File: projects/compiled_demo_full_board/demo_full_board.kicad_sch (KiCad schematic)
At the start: 16 parts, among them U1 ATmega328, U2 LM7805, Y1 16MHz

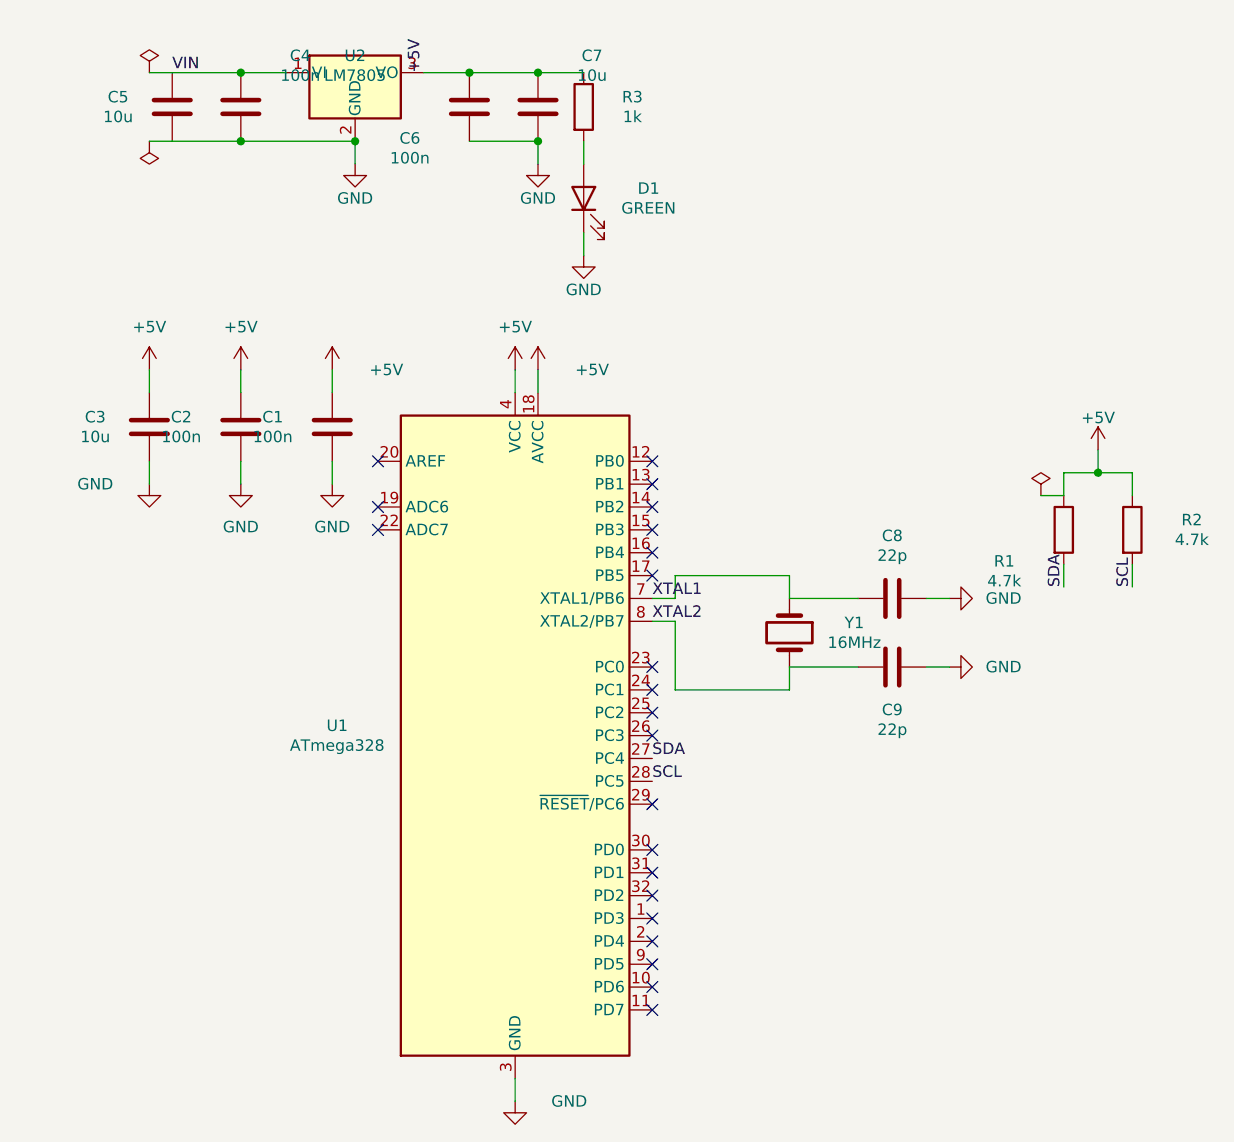
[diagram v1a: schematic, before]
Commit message: Body model sees real symbol graphics; quiet nets drop junction tags
User-reported flaws from visual review, both fixed at the root:

- Wires over symbol artwork: the body model was pin-derived and blind to
  drawn graphics — an op-amp triangle's vertices stick out beyond the pin
  box, so "legal" wires crossed the drawing. internal/sexp/graphics.go now
  parses rectangle/polyline/circle/arc/bezier extents per unit with the
  exact pin transform; metrics.BodyBBox unions them with the legacy box,
  clamped off pin tips (Device:LED's emission arrows overhang the cathode
  pin and would have swallowed it). NE5532 feedback: 8 stroke crossings
  through the triangle before, 0 after (loops now label pairs). The model
  also exposed genuinely bad baked geometry in mcu_minimal_atmega328's
  crystal — repositioned with the template contract intact.

- "ANODE" tag on a resistor leg: net names with a "_" prefix are now
  quiet — connectivity only, their documentation label is stripped at the
  end of compilation when the wiring alone keeps the net whole. Junction
  nodes (R->LED) stay unlabeled like in any hand-drawn schematic.

- Battery hump: led_18650 anchors R1 in the pin's exit direction; the
  design guide gains the "respect the pin's exit direction" and "internal
  junctions carry no tag" recipes.

Co-Authored-By: Claude Fable 5 <noreply@anthropic.com>
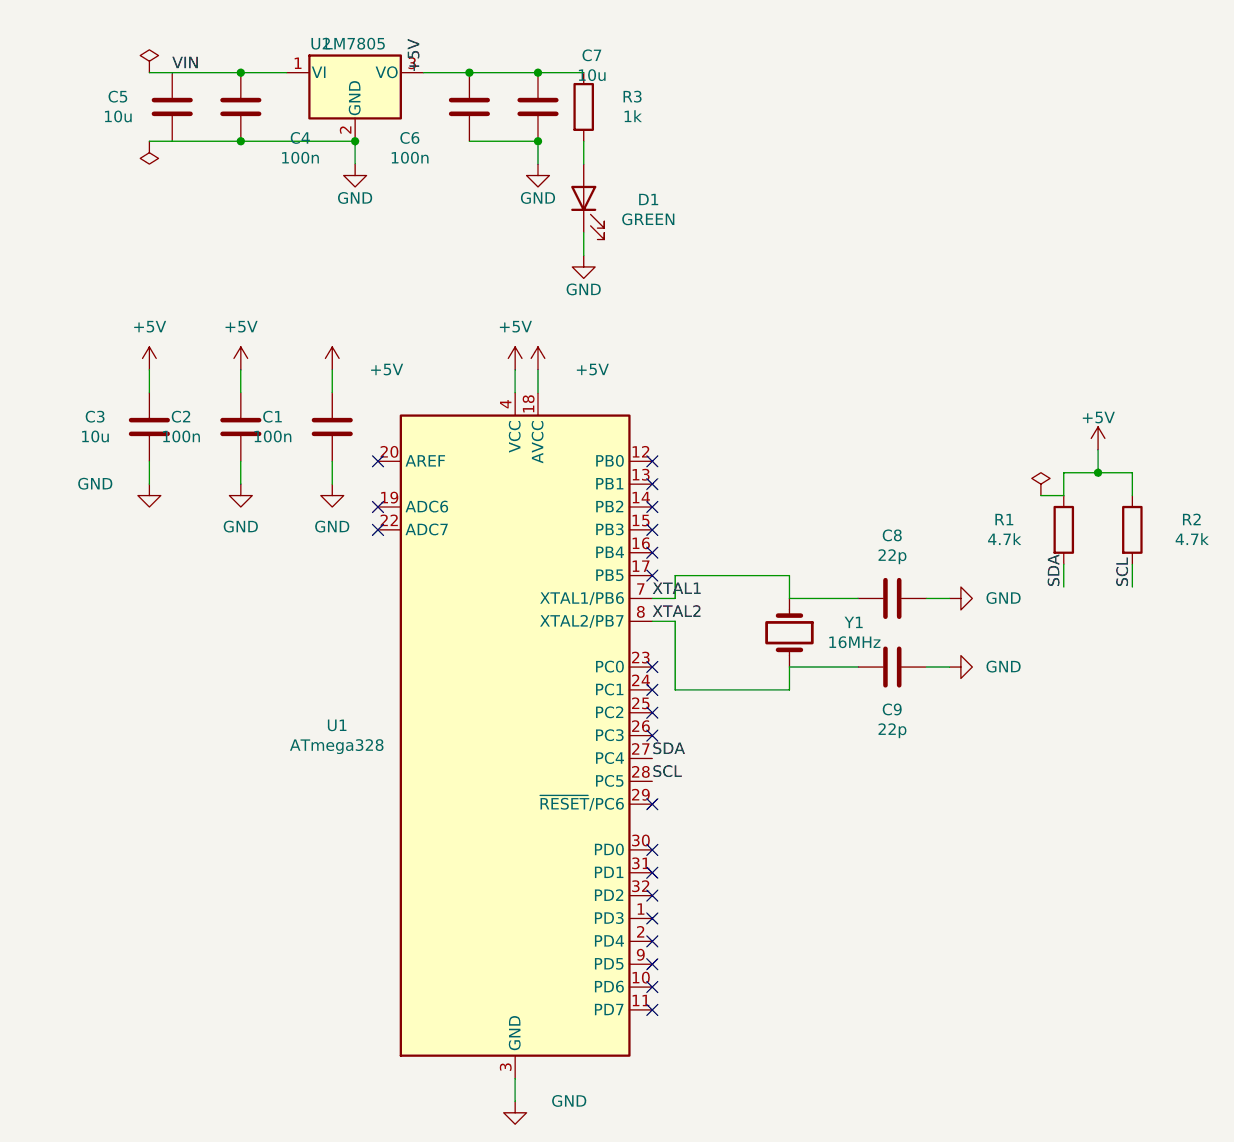
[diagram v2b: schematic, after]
